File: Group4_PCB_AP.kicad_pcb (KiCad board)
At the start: 2 copper layers, 70 x 70 mm, 97 parts, among them J18 Conn_Coaxial, J19 Conn_Coaxial, J20 Conn_02x02_Odd_Even, J21 Conn_02x02_Odd_Even, J22 Conn_Coaxial, J23 Conn_Coaxial, J24 Conn_02x02_Odd_Even, J25 Conn_02x02_Odd_Even, J26 Conn_02x02_Odd_Even, J27 Conn_02x02_Odd_Even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

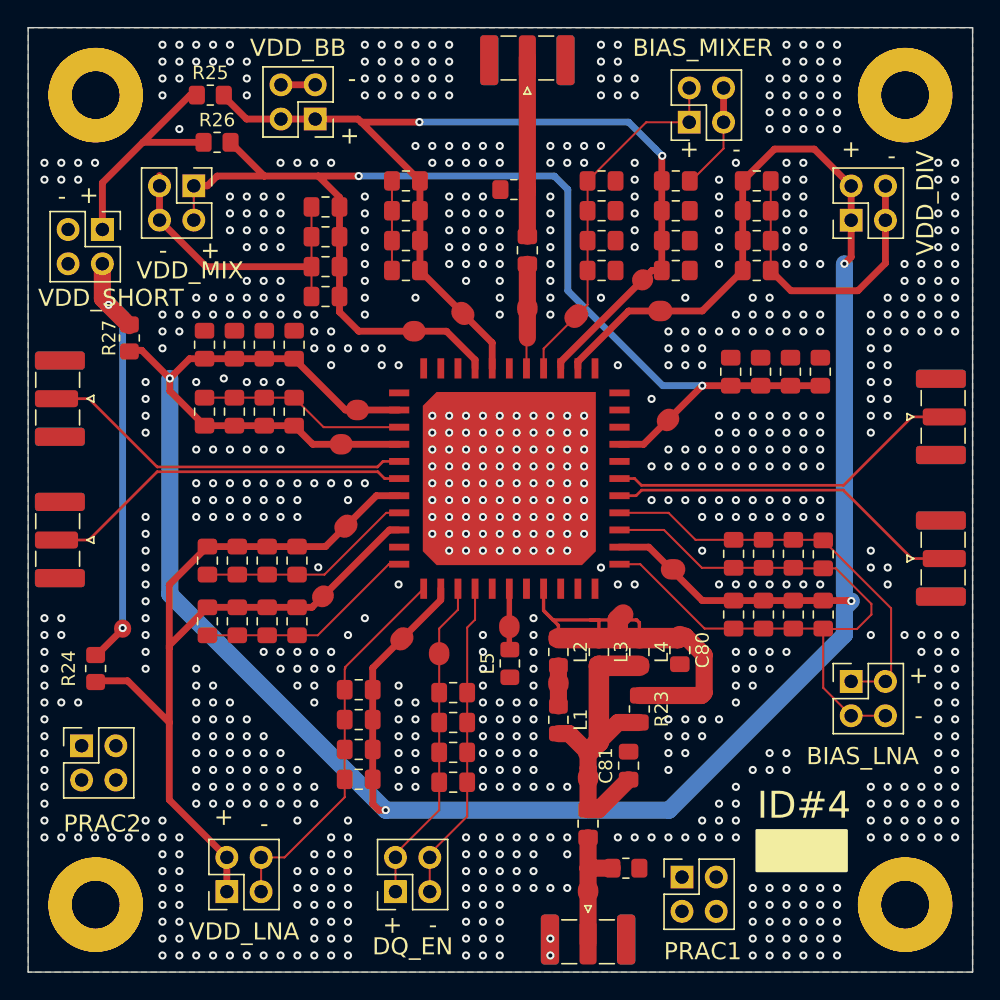
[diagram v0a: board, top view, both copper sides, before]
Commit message: Cleaned up matching network
Cleaned up schematic and layout for matching network, removed termination and 0 ohm resistors, removed probe points on all RF traces. Removed zero ohm from VSOURCE
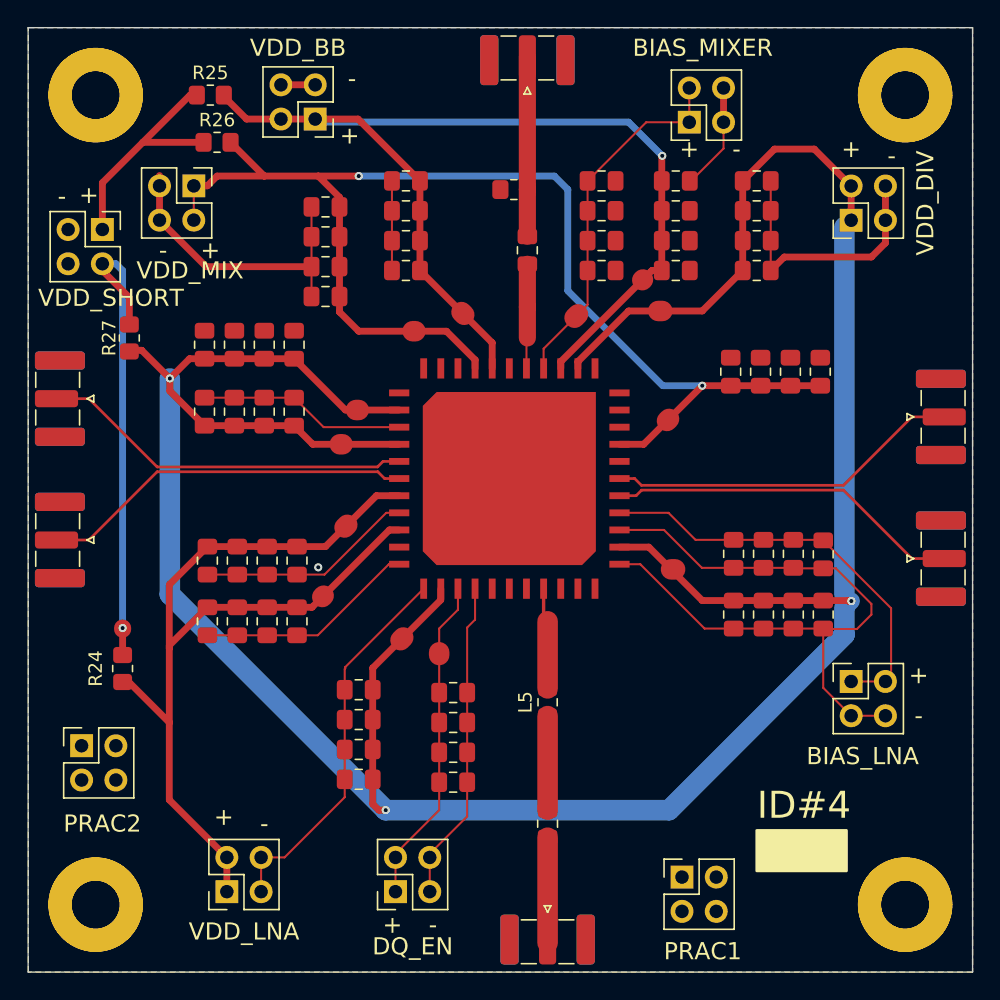
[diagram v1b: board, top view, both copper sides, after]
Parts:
- removed C80, C81: 1n, Capacitor_SMD:C_0805_2012Metric_Pad1.18x1.45mm_HandSolder
- removed L2, L3, L4: L, Inductor_SMD:L_0805_2012Metric_Pad1.15x1.40mm_HandSolder
- removed the L5 at (206.2, 109.6)
- removed R20: 50, Resistor_SMD:R_0805_2012Metric_Pad1.20x1.40mm_HandSolder
- removed R23: 0, Resistor_SMD:R_0805_2012Metric_Pad1.20x1.40mm_HandSolder
- moved C76 3.00 mm to (209.0, 121.5)
- moved J19 3.00 mm to (209.0, 130.3)
- moved R24 2.00 mm to (177.5, 110.0)
- moved L5 1.53 mm to (209.0, 112.5), turned to 90 degrees
- renumbered L1 to L5
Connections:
- net /CK_CHIP renamed /CK_BOARD
- L5 pad 1: Net-(L1-Pad1) -> /VIN_RF_S
- L5 pad 2: /VIN_RF_S -> /VIN_RF
- U1 pad 12: /VSOURCE -> /GND
- U1 pad 13: /VSOURCE -> /GND
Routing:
- net /VIN_RF: track 35.6 -> 7.51 mm
- net /VIN_RF_S: track 24.5 -> 6.94 mm
- net /VSOURCE: track 4.53 -> 0.00 mm
- net /VDD_BB: track 76.1 -> 79.6 mm, vias 2 -> 1
- net Net-(L1-Pad1): track 3.18 -> 0.00 mm
- net /VDD: track 50.5 -> 53.4 mm, vias 2 -> 1
- net /GND: track 215.1 -> 213.0 mm, vias 845 -> 1
- net /VDD_LNA: track 71.8 -> 69.8 mm
- net /SMA_VIN_RF: track 9.80 -> 7.80 mm
- net /VDD_DIV: vias 4 -> 3

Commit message: fixed up some caps, 4mm away from chip. need to check if the adjcaent caps r too close
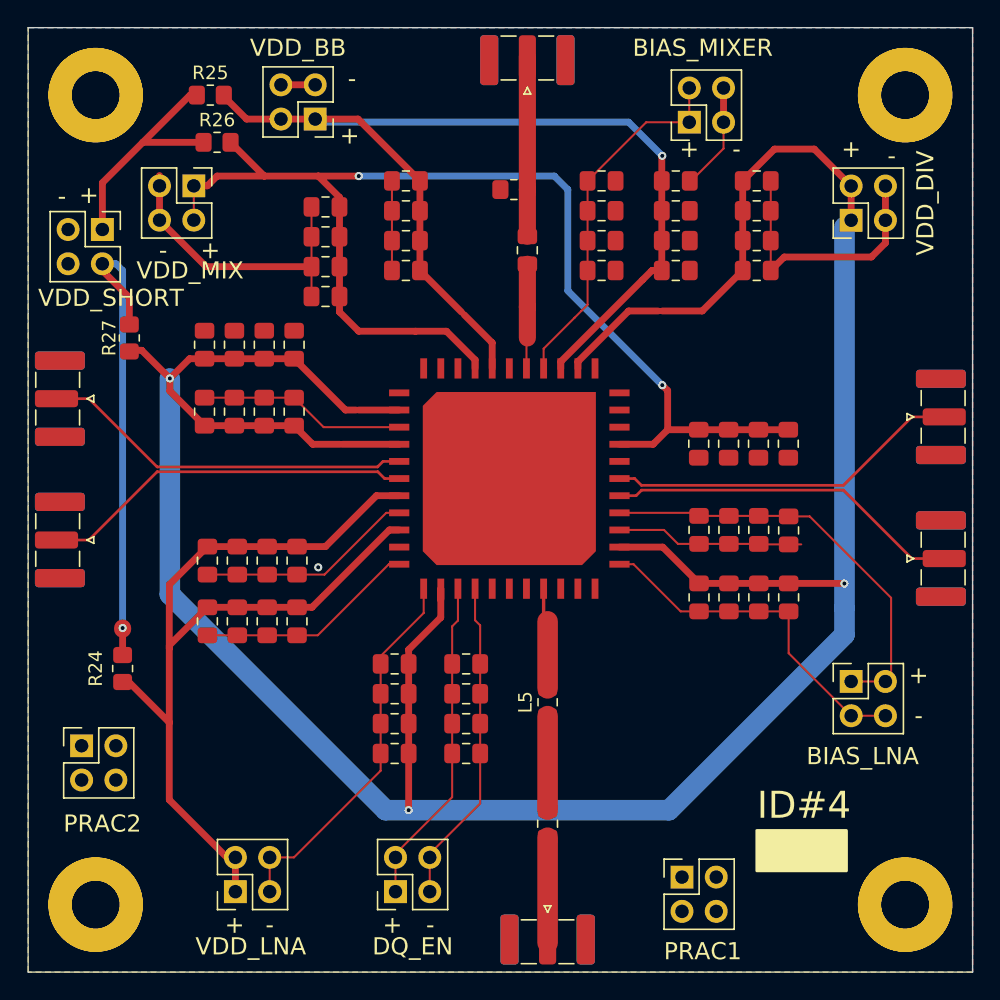
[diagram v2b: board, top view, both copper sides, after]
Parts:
- moved C43 10.5 mm to (220.2, 93.3), turned to -90 degrees
- moved C41 7.04 mm to (222.4, 93.3), turned to -90 degrees
- moved C37 6.84 mm to (226.8, 93.3), turned to -90 degrees
- moved C39 5.34 mm to (224.6, 93.3), turned to -90 degrees
- moved C72 3.28 mm to (197.7, 109.7)
- moved C73 3.28 mm to (197.7, 111.9)
- moved C74 3.28 mm to (197.7, 114.1)
- moved C75 3.28 mm to (197.7, 116.3)
- moved C20 3.12 mm to (220.2, 99.7)
- moved C21 3.12 mm to (222.4, 99.7)
- moved C22 3.12 mm to (224.7, 99.7)
- moved C23 3.12 mm to (226.9, 99.8)
- moved C64 2.86 mm to (220.2, 104.7)
- moved C66 2.86 mm to (222.4, 104.7)
- moved C68 2.86 mm to (224.7, 104.7)
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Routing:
- net /GND: track 213.0 -> 200.5 mm
- net /VDD_DIV: track 225.7 -> 221.7 mm
- net /VDD_MIX: track 94.7 -> 91.4 mm

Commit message: finished rerouting
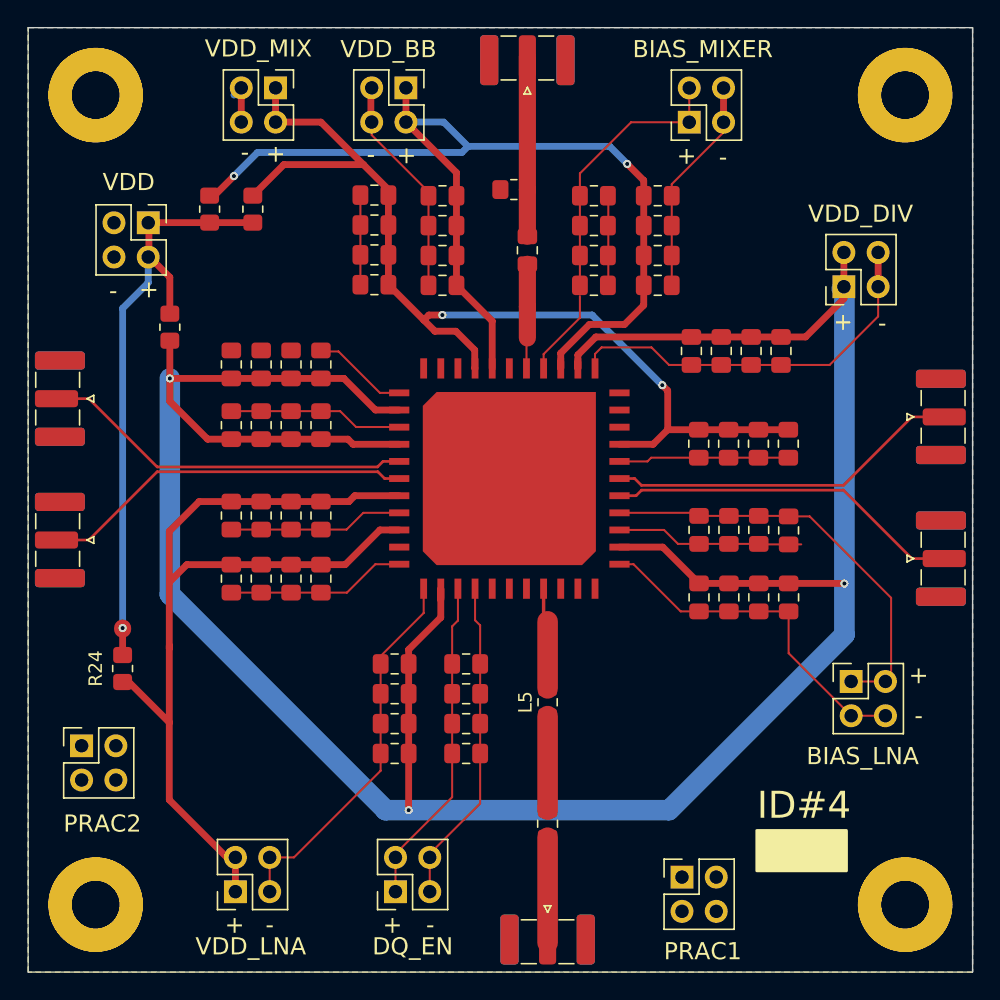
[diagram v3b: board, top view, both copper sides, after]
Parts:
- moved C50 12.7 mm to (226.3, 86.5), turned to -90 degrees
- moved C48 10.4 mm to (224.1, 86.5), turned to -90 degrees
- moved J25 9.46 mm to (188.8, 67.0)
- moved C46 8.59 mm to (221.9, 86.5), turned to -90 degrees
- moved R25 8.45 mm to (183.9, 76.0), turned to 90 degrees
- moved C44 7.68 mm to (219.7, 86.5), turned to -90 degrees
- moved J27 7.11 mm to (198.5, 67.0), turned to -90 degrees
- moved R26 5.61 mm to (187.2, 76.0), turned to 90 degrees
- moved J26 4.95 mm to (231.0, 81.7)
- moved C29 3.78 mm to (192.2, 98.7)
- moved C31 3.78 mm to (190.0, 98.7)
- moved C33 3.78 mm to (187.8, 98.7)
- moved C35 3.78 mm to (185.6, 98.7)
- moved C36 3.73 mm to (196.2, 81.6)
- moved C38 3.73 mm to (196.2, 79.3)
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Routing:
- net /GND: track 200.5 -> 230.6 mm, vias 1 -> 0
- net /VDD_MIX: track 91.4 -> 75.3 mm
- net /VDD_DIV: track 221.7 -> 207.3 mm
- net /VDD: track 53.4 -> 46.3 mm
- net /VDD_BB: track 79.2 -> 82.6 mm, vias 1 -> 2
- net /VDD_LNA: track 69.6 -> 70.2 mm

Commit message: fixed DRC except ONE; added via stitching; need to do test points
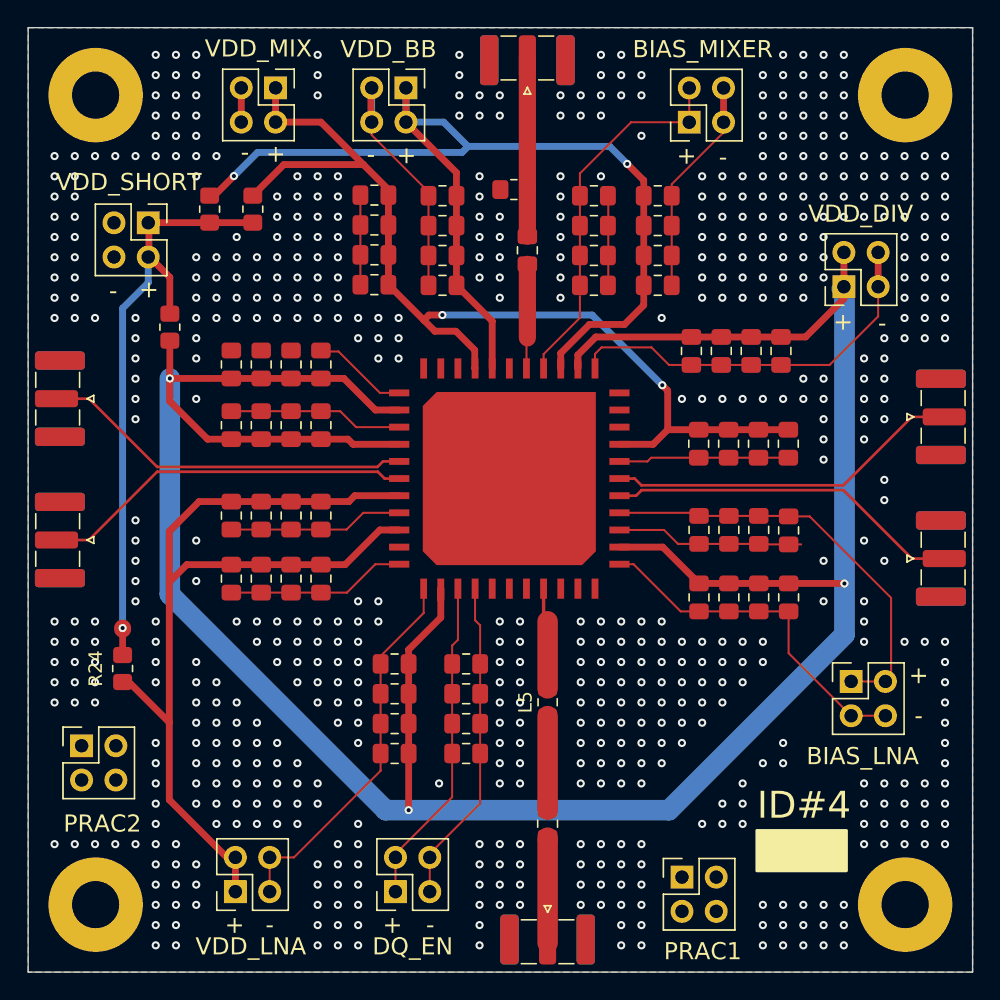
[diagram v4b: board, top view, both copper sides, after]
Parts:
- removed the ? at (235.5, 67.5)
- removed the ? at (175.5, 127.5)
- removed the ? at (235.5, 127.5)
- removed the ? at (175.5, 67.5)
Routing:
- net /VDD_BB: track 82.6 -> 85.1 mm
- net /GND: track 230.6 -> 232.1 mm, vias 0 -> 612

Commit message: Fixed final DRC error
DRC clean and added probe points
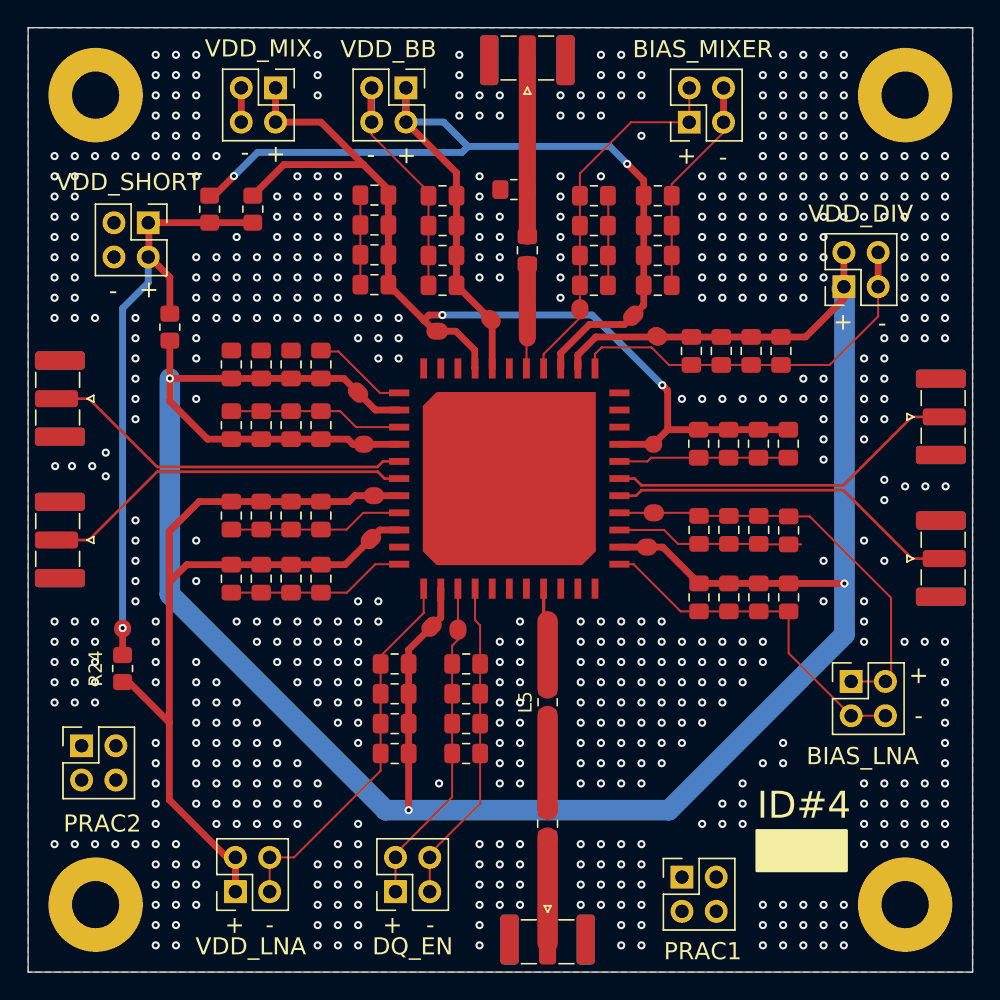
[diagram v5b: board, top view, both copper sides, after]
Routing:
- net /GND: vias 612 -> 617

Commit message: Added UCLA Silk Screen and Gerber files
Finalized PCB and made Gerber files
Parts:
- added G***: LOGO, LOGO, F.Cu at (227.5, 128.8)
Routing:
- net /GND: vias 617 -> 602
